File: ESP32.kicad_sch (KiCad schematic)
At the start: 1 part, among them U1 ESP32-S3-MINI-1

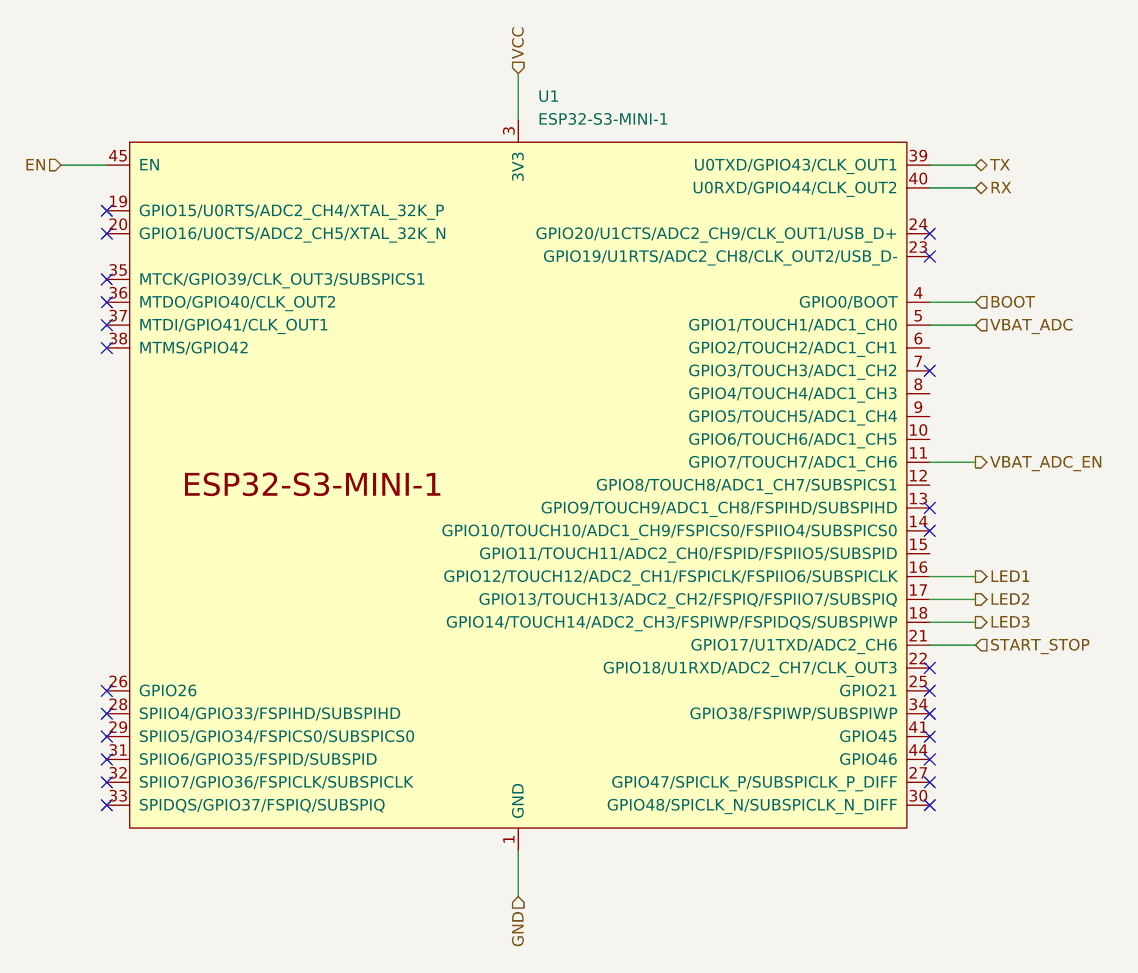
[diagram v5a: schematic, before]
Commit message: replace GND heriarchical labels with GND symbols
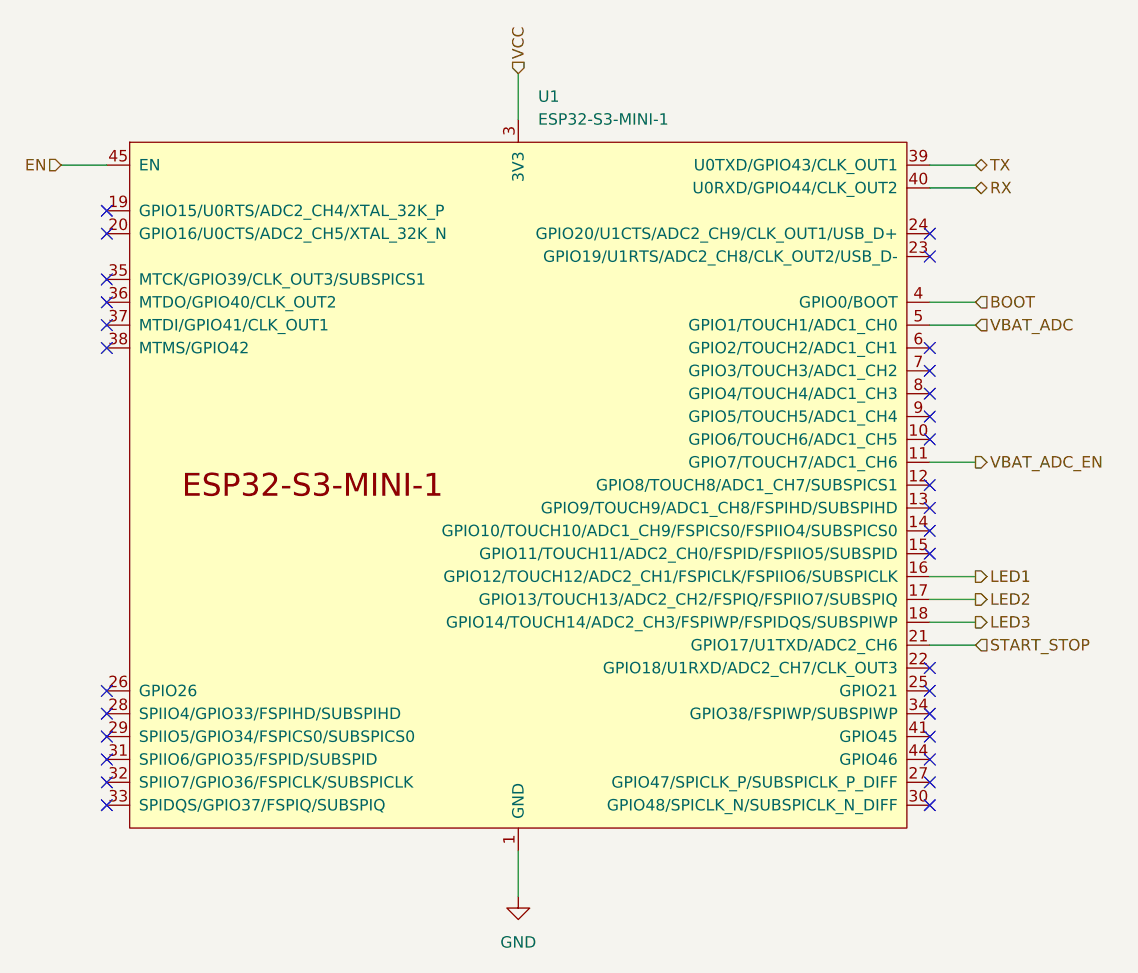
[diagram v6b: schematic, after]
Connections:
- no-connect marks 24 -> 30
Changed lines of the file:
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@@
   (no_connect (at 193.04 130.81))
   (no_connect (at 101.6 120.65))
+  (no_connect (at 193.04 82.55))
   (no_connect (at 193.04 125.73))
   (no_connect (at 101.6 128.27))
@@
   (no_connect (at 101.6 82.55))
   (no_connect (at 101.6 77.47))
+  (no_connect (at 193.04 92.71))
   (no_connect (at 193.04 69.85))
+  (no_connect (at 193.04 90.17))
   (no_connect (at 101.6 67.31))
   (no_connect (at 193.04 102.87))
+  (no_connect (at 193.04 87.63))
   (no_connect (at 101.6 80.01))
+  (no_connect (at 193.04 105.41))
   (no_connect (at 101.6 74.93))
   (no_connect (at 193.04 118.11))
   (no_connect (at 101.6 125.73))
   (no_connect (at 101.6 69.85))
+  (no_connect (at 193.04 97.79))
   (no_connect (at 193.04 128.27))
   (wire (pts (xy 193.04 80.01) (xy 198.12 80.01))
@@
     (effects (font (size 1.27 1.27)) (justify left))
   )
-  (hierarchical_label "GND" (shape input) (at 147.32 143.51 270) (fields_autoplaced)
-    (effects (font (size 1.27 1.27)) (justify right))
-  )
   (hierarchical_label "LED1" (shape output) (at 198.12 107.95 0) (fields_autoplaced)
     (effects (font (size 1.27 1.27)) (justify left))
@@
     (effects (font (size 1.27 1.27)) (justify left))
   )
+  (symbol (lib_id "power:GND") (at 147.32 143.51 0) (unit 1)
+    (in_bom yes) (on_board yes) (dnp no) (fields_autoplaced)
+    (property "Reference" "#PWR04" (at 147.32 149.86 0)
+      (effects (font (size 1.27 1.27)) hide)
+    )
+    (property "Value" "GND" (at 147.32 148.59 0)
+      (effects (font (size 1.27 1.27)))
+    )
+    (property "Footprint" "" (at 147.32 143.51 0)
+      (effects (font (size 1.27 1.27)) hide)
+    )
+    (property "Datasheet" "" (at 147.32 143.51 0)
+      (effects (font (size 1.27 1.27)) hide)
+    )
+    (pin "1")
+    (instances
+      (project "key-fob-pcb"
+        (path "/b002c3bf-fc58-4993-80f7-7914d3aa1ac9/53196cbc-427d-42ed-8e9a-570bc17b7f6f"
+          (reference "#PWR04") (unit 1)
+        )
+      )
+    )
+  )
   (symbol (lib_id "PCM_Espressif:ESP32-S3-MINI-1") (at 147.32 97.79 0) (unit 1)

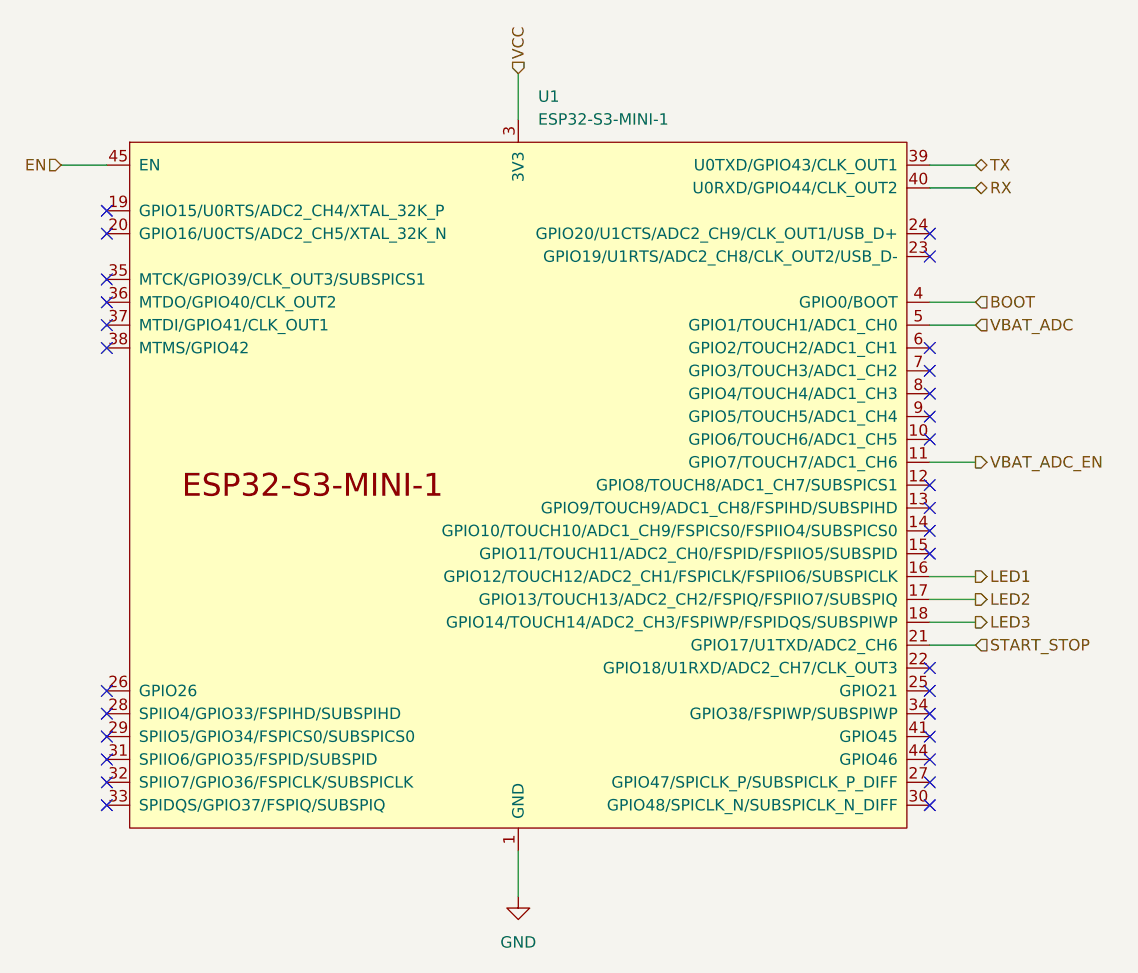
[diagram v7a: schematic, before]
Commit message: switched to full-sized ESP32 S3 WROOM and redid PCB layout
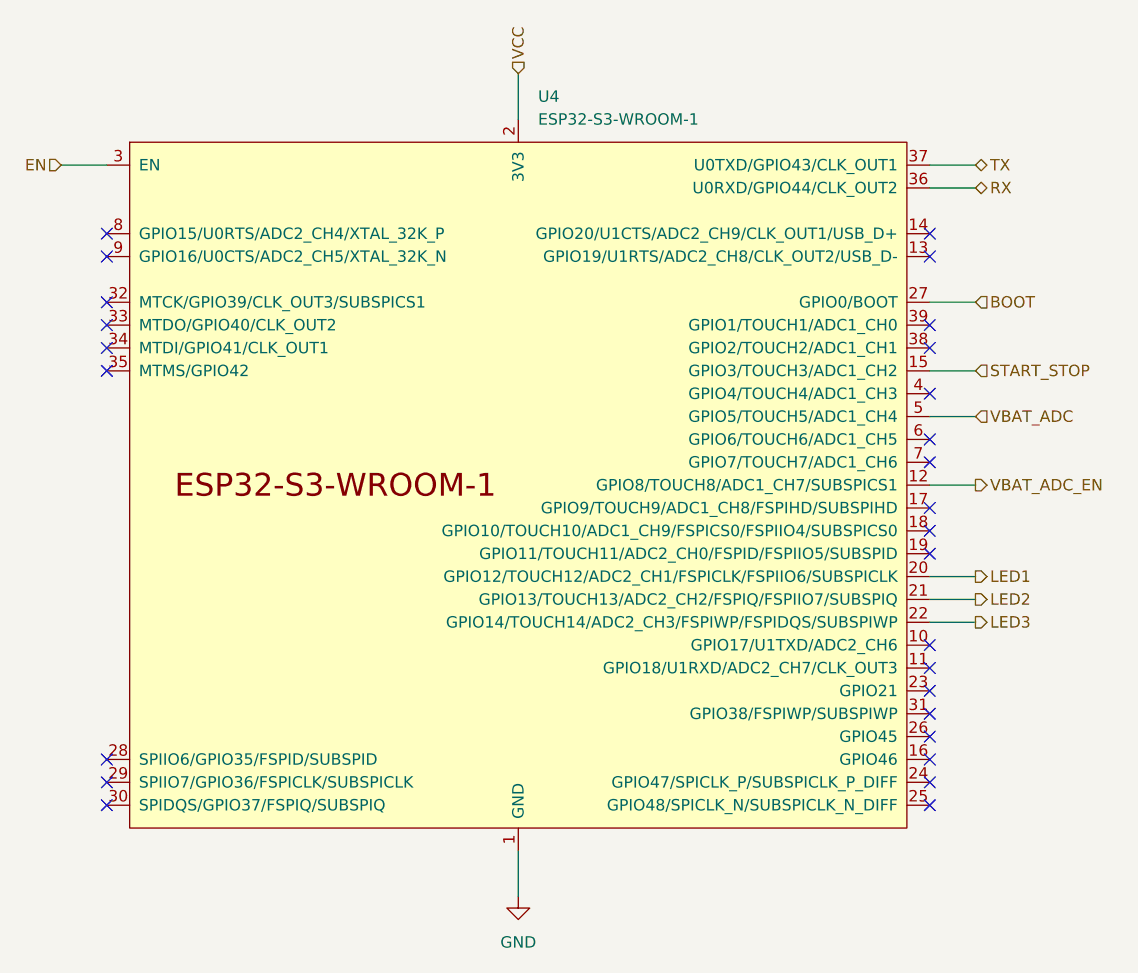
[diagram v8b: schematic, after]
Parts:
- removed U1: ESP32-S3-MINI-1, PCM_Espressif:ESP32-S3-MINI-1, symbol PCM_Espressif:ESP32-S3-MINI-1
- added U4: ESP32-S3-WROOM-1, PCM_Espressif:ESP32-S3-WROOM-1, symbol PCM_Espressif:ESP32-S3-WROOM-1
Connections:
- net BOOT: now also U4.27 (GPIO0/BOOT)
- net EN: now also U4.3 (EN)
- net GND: now also U4.1 (GND), U4.40 (GND), U4.41 (GND)
- net LED1: now also U4.20 (GPIO12/TOUCH12/ADC2_CH1/FSPICLK/FSPIIO6/SUBSPICLK)
- net LED2: now also U4.21 (GPIO13/TOUCH13/ADC2_CH2/FSPIQ/FSPIIO7/SUBSPIQ)
- net LED3: now also U4.22 (GPIO14/TOUCH14/ADC2_CH3/FSPIWP/FSPIDQS/SUBSPIWP)
- net RX: now also U4.36 (U0RXD/GPIO44/CLK_OUT2)
- net START_STOP: now also U4.15 (GPIO3/TOUCH3/ADC1_CH2)
- net TX: now also U4.37 (U0TXD/GPIO43/CLK_OUT1)
- net VBAT_ADC: now also U4.5 (GPIO5/TOUCH5/ADC1_CH4)
- net VBAT_ADC_EN: now also U4.12 (GPIO8/TOUCH8/ADC1_CH7/SUBSPICS1)
- net VCC: now also U4.2 (3V3)
- no-connect marks 30 -> 27
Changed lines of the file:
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@@
   )
   (no_connect (at 193.04 100.33))
-  (no_connect (at 193.04 85.09))
-  (no_connect (at 101.6 123.19))
   (no_connect (at 193.04 120.65))
   (no_connect (at 101.6 133.35))
   (no_connect (at 193.04 123.19))
   (no_connect (at 193.04 130.81))
-  (no_connect (at 101.6 120.65))
   (no_connect (at 193.04 82.55))
   (no_connect (at 193.04 125.73))
+  (no_connect (at 193.04 80.01))
   (no_connect (at 101.6 128.27))
   (no_connect (at 193.04 133.35))
+  (no_connect (at 193.04 115.57))
   (no_connect (at 193.04 72.39))
   (no_connect (at 101.6 130.81))
-  (no_connect (at 101.6 82.55))
-  (no_connect (at 101.6 77.47))
+  (no_connect (at 101.6 85.09))
+  (no_connect (at 101.6 80.01))
   (no_connect (at 193.04 92.71))
   (no_connect (at 193.04 69.85))
-  (no_connect (at 193.04 90.17))
-  (no_connect (at 101.6 67.31))
+  (no_connect (at 101.6 69.85))
   (no_connect (at 193.04 102.87))
   (no_connect (at 193.04 87.63))
-  (no_connect (at 101.6 80.01))
+  (no_connect (at 101.6 82.55))
   (no_connect (at 193.04 105.41))
-  (no_connect (at 101.6 74.93))
+  (no_connect (at 101.6 77.47))
   (no_connect (at 193.04 118.11))
-  (no_connect (at 101.6 125.73))
-  (no_connect (at 101.6 69.85))
-  (no_connect (at 193.04 97.79))
+  (no_connect (at 193.04 95.25))
+  (no_connect (at 101.6 72.39))
   (no_connect (at 193.04 128.27))
-  (wire (pts (xy 193.04 80.01) (xy 198.12 80.01))
-    (stroke (width 0) (type default))
-  )
   (wire (pts (xy 193.04 113.03) (xy 198.12 113.03))
     (stroke (width 0) (type default))
@@
     (stroke (width 0) (type default))
   )
-  (wire (pts (xy 193.04 95.25) (xy 198.12 95.25))
-    (stroke (width 0) (type default))
-  )
-  (wire (pts (xy 193.04 115.57) (xy 198.12 115.57))
+  (wire (pts (xy 193.04 90.17) (xy 198.12 90.17))
     (stroke (width 0) (type default))
   )
   (wire (pts (xy 147.32 52.07) (xy 147.32 57.15))
+    (stroke (width 0) (type default))
+  )
+  (wire (pts (xy 193.04 97.79) (xy 198.12 97.79))
     (stroke (width 0) (type default))
   )
@@
     (stroke (width 0) (type default))
   )
+  (wire (pts (xy 193.04 85.09) (xy 198.12 85.09))
+    (stroke (width 0) (type default))
+  )
   (wire (pts (xy 147.32 138.43) (xy 147.32 143.51))
     (stroke (width 0) (type default))
   )
-  (hierarchical_label "VBAT_ADC" (shape input) (at 198.12 80.01 0) (fields_autoplaced)
+  (hierarchical_label "VBAT_ADC" (shape input) (at 198.12 90.17 0) (fields_autoplaced)
     (effects (font (size 1.27 1.27)) (justify left))
   )
@@
     (effects (font (size 1.27 1.27)) (justify left))
   )
-  (hierarchical_label "START_STOP" (shape input) (at 198.12 115.57 0) (fields_autoplaced)
+  (hierarchical_label "START_STOP" (shape input) (at 198.12 85.09 0) (fields_autoplaced)
     (effects (font (size 1.27 1.27)) (justify left))
   )
@@
     (effects (font (size 1.27 1.27)) (justify left))
   )
-  (hierarchical_label "VBAT_ADC_EN" (shape output) (at 198.12 95.25 0) (fields_autoplaced)
+  (hierarchical_label "VBAT_ADC_EN" (shape output) (at 198.12 97.79 0) (fields_autoplaced)
     (effects (font (size 1.27 1.27)) (justify left))
   )
@@
     )
   )
-  (symbol (lib_id "PCM_Espressif:ESP32-S3-MINI-1") (at 147.32 97.79 0) (unit 1)
+  (symbol (lib_id "PCM_Espressif:ESP32-S3-WROOM-1") (at 147.32 97.79 0) (unit 1)
     (in_bom yes) (on_board yes) (dnp no) (fields_autoplaced)
-    (property "Reference" "U1" (at 149.5141 54.61 0)
+    (property "Reference" "U4" (at 149.5141 54.61 0)
       (effects (font (size 1.27 1.27)) (justify left))
     )
-    (property "Value" "ESP32-S3-MINI-1" (at 149.5141 57.15 0)
+    (property "Value" "ESP32-S3-WROOM-1" (at 149.5141 57.15 0)
       (effects (font (size 1.27 1.27)) (justify left))
     )
-    (property "Footprint" "PCM_Espressif:ESP32-S3-MINI-1" (at 147.32 153.67 0)
+    (property "Footprint" "PCM_Espressif:ESP32-S3-WROOM-1" (at 149.86 146.05 0)
       (effects (font (size 1.27 1.27)) hide)
     )
-    (property "Datasheet" "https://www.espressif.com/sites/default/files/documentation/esp32-s3-mini-1_mini-1u_datasheet_en.pdf" (at 147.32 156.21 0)
-      (effects (font (size 1.27 1.27)) hide)
-    )
-    (property "MPN" "C2913206" (at 147.32 97.79 0)
+    (property "Datasheet" "https://www.espressif.com/sites/default/files/documentation/esp32-s3-wroom-1_wroom-1u_datasheet_en.pdf" (at 149.86 148.59 0)
       (effects (font (size 1.27 1.27)) hide)
     )
@@
     (pin "40")
     (pin "41")
-    (pin "42")
-    (pin "43")
-    (pin "44")
-    (pin "45")
-    (pin "46")
-    (pin "47")
-    (pin "48")
-    (pin "49")
     (pin "5")
-    (pin "50")
-    (pin "51")
-    (pin "52")
-    (pin "53")
-    (pin "54")
-    (pin "55")
-    (pin "56")
-    (pin "57")
-    (pin "58")
-    (pin "59")
     (pin "6")
-    (pin "60")
-    (pin "61")
-    (pin "62")
-    (pin "63")
-    (pin "64")
-    (pin "65")
     (pin "7")
     (pin "8")
@@
       (project "key-fob-pcb"
         (path "/b002c3bf-fc58-4993-80f7-7914d3aa1ac9/53196cbc-427d-42ed-8e9a-570bc17b7f6f"
-          (reference "U1") (unit 1)
+          (reference "U4") (unit 1)
         )
       )
